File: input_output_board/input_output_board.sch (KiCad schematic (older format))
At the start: 18 parts, among them J1 Neutrik_NCJ6FA-H, J2 Neutrik_NCJ6FA-H, J3 Neutrik_NCJ6FA-H, J4 Neutrik_NCJ6FA-H, J5 AudioJack3, J6 Conn_02x05_Odd_Even, J7 Molex_SL_01x04_Male, J8 Molex_SL_01x04_Male, K1 G6S-2, K2 G6S-2, K3 G6S-2, K4 G6S-2, K5 G6S-2

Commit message: remove shield from internal audio connectors, change internal audio connectors to 1x2, and split input shields into four separate nets (one for each input)
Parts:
- J7: value Molex_SL_01x04_Male -> Molex_SL_01x02_Male; footprint Connector_Molex_SL:Molex_SL_A-70543-0003_1x04_P2.54mm_Vertical -> Connector_Molex_SL:Molex_SL_A-70543-0001_1x02_P2.54mm_Vertical; symbol Connector_gkeeth:Molex_SL_01x04_Male -> Connector_gkeeth:Molex_SL_01x02_Male; Distributor PN WM4802-ND -> (none); URL https://www.digikey.com/products/en?keywords=0705430003 -> (none); Unit Price 0.99 -> (none)
- J8: value Molex_SL_01x04_Male -> Molex_SL_01x02_Male; footprint Connector_Molex_SL:Molex_SL_A-70543-0003_1x04_P2.54mm_Vertical -> Connector_Molex_SL:Molex_SL_A-70543-0001_1x02_P2.54mm_Vertical; symbol Connector_gkeeth:Molex_SL_01x04_Male -> Connector_gkeeth:Molex_SL_01x02_Male; Distributor PN WM4802-ND -> (none); Manufacturer PN 0705430003 -> 0705430001; URL https://www.digikey.com/products/en?keywords=0705430003 -> (none); Unit Price 0.99 -> (none)
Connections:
- net input_selected_cold: now also J7.2 (Pin_2); no longer J7.4 (Pin_4)
- net output_cold: now also J8.2 (Pin_2); no longer J8.4 (Pin_4)
- net output_shield: no longer J8.2 (Pin_2), J8.3 (Pin_3)
- removed net input_shield: J1.1, J1.G, J1.S, J2.1, J2.G, J2.S, J3.1, J3.G, J3.S, J4.1, J4.G, J4.S, J7.2 (Pin_2), J7.3 (Pin_3)
- new net input1_shield: J1.1, J1.G, J1.S
- new net input2_shield: J2.1, J2.G, J2.S
- new net input3_shield: J3.1, J3.G, J3.S
- new net input4_shield: J4.1, J4.G, J4.S
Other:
- note added: "Shields & XLR case ground bonded DIRECTLY to chassis at each connector:\n - XLR combo connectors via mounting screw holes\n - phono jack via chassis contact\n\nflood input_shield across all inputs"
- note added: "output shield connected to chassis by output connector"
- note removed: "Shields & XLR case ground bonded DIRECTLY to chassis at each connector:\n - XLR combo connectors via mounting screw holes\n - phono jack via chassis contact\n\nflood input_shield across all inputs and connect to input connector (J7)"
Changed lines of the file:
@@
 	2450 3750 2450 3850
 Text Label 2000 5200 2    50   ~ 0
-input_shield
+input3_shield
 Text Label 2900 5200 0    50   ~ 0
 input3_hot
@@
 	2150 5200 2050 5200
 Wire Wire Line
-	8200 5850 7300 5850
+	8200 5650 7300 5650
 Text Label 7500 5550 0    50   ~ 0
 output_hot
-Text Label 7500 5850 0    50   ~ 0
+Text Label 7500 5650 0    50   ~ 0
 output_cold
-Wire Wire Line
-	7300 5750 7400 5750
-Wire Wire Line
-	7300 5650 7400 5650
-Wire Wire Line
-	7400 5650 7400 5750
-Connection ~ 7400 5750
-Wire Wire Line
-	7400 5750 8050 5750
-Text Label 7500 5750 0    50   ~ 0
-output_shield
 Wire Wire Line
 	2000 1600 1400 1600
@@
 $EndComp
 $Comp
-L Connector_gkeeth:Molex_SL_01x04_Male J7
+L Connector_gkeeth:Molex_SL_01x02_Male J7
 U 1 1 5CB530B8
-P 6500 4250
-F 0 "J7" H 6472 4224 50  0000 R CNN
-F 1 "Molex_SL_01x04_Male" H 6472 4133 50  0000 R CNN
-F 2 "Connector_Molex_SL:Molex_SL_A-70543-0003_1x04_P2.54mm_Vertical" H 6500 4250 50  0001 C CNN
-F 3 "https://www.molex.com/pdm_docs/sd/705430001_sd.pdf" H 6500 4250 50  0001 C CNN
-F 4 "Molex" H 6500 4250 50  0001 C CNN "Manufacturer"
-F 5 "0705430003" H 6500 4250 50  0001 C CNN "Manufacturer PN"
-F 6 "Digikey" H 6500 4250 50  0001 C CNN "Distributor"
-F 7 "WM4802-ND" H 6500 4250 50  0001 C CNN "Distributor PN"
-F 8 "https://www.digikey.com/products/en?keywords=0705430003" H 6500 4250 50  0001 C CNN "URL"
-F 9 "0.99" H 6500 4250 50  0001 C CNN "Unit Price"
-	1    6500 4250
+P 6500 4150
+F 0 "J7" H 6472 4124 50  0000 R CNN
+F 1 "Molex_SL_01x02_Male" H 6472 4033 50  0000 R CNN
+F 2 "Connector_Molex_SL:Molex_SL_A-70543-0001_1x02_P2.54mm_Vertical" H 6500 4150 50  0001 C CNN
+F 3 "https://www.molex.com/pdm_docs/sd/705430001_sd.pdf" H 6500 4150 50  0001 C CNN
+F 4 "Molex" H 6500 4150 50  0001 C CNN "Manufacturer"
+F 5 "0705430003" H 6500 4150 50  0001 C CNN "Manufacturer PN"
+F 6 "Digikey" H 6500 4150 50  0001 C CNN "Distributor"
+	1    6500 4150
 	-1   0    0    -1
 $EndComp
 Text Label 5450 4250 0    50   ~ 0
-input_shield
-Wire Wire Line
-	6200 4250 6300 4250
-Connection ~ 6200 4250
-Wire Wire Line
-	6200 4350 6300 4350
-Wire Wire Line
-	6200 4250 6200 4350
-Text Label 5450 4450 0    50   ~ 0
 input_selected_cold
 Text Label 5450 4150 0    50   ~ 0
 input_selected_hot
 Text Label 2000 3450 2    50   ~ 0
-input_shield
+input2_shield
 Text Label 2000 3250 2    50   ~ 0
 input2_hot
@@
 input3_hot
 Text Label 2000 1700 2    50   ~ 0
-input_shield
+input1_shield
 Text Label 2000 1600 2    50   ~ 0
 input1_cold
@@
 	9200 5750 9400 5750
 Wire Wire Line
-	8200 5850 8200 5950
+	8200 5650 8200 5950
 Wire Wire Line
 	8200 5950 8400 5950
@@
 	7300 5550 8400 5550
 Wire Wire Line
-	8050 5750 8050 6350
-Wire Wire Line
-	8050 6350 9300 6350
-Wire Wire Line
-	9300 6350 9300 5850
+	8050 6450 9300 6450
+Wire Wire Line
+	9300 6450 9300 5850
 Wire Wire Line
 	9300 5850 9400 5850
@@
 Connection ~ 8200 2650
 Text Notes 7500 3950 0    50   ~ 0
-Shields & XLR case ground bonded DIRECTLY to chassis at each connector:\n - XLR combo connectors via mounting screw holes\n - phono jack via chassis contact\n\nflood input_shield across all inputs and connect to input connector (J7)
+Shields & XLR case ground bonded DIRECTLY to chassis at each connector:\n - XLR combo connectors via mounting screw holes\n - phono jack via chassis contact\n\nflood input_shield across all inputs
 Wire Wire Line
 	2350 2100 2350 2000
@@
 	2050 7350 2350 7350
 Text Label 2000 6950 2    50   ~ 0
-input_shield
+input4_shield
 Wire Wire Line
 	2450 7250 2450 7350
@@
 	5000 2000 4300 2000
 Wire Wire Line
-	6300 4450 5000 4450
+	6300 4250 5000 4250
 Text Notes 700  7850 0    79   Italic 16
 INPUT CONNECTORS / RELAYS
@@
 Wire Notes Line
 	650  7900 650  550
-Wire Wire Line
-	5450 4250 6200 4250
 Wire Notes Line
 	750  2300 750  650
@@
 	5650 4850 5650 7900
 Wire Wire Line
-	5000 5500 5000 4450
-Connection ~ 5000 4450
+	5000 5500 5000 4250
+Connection ~ 5000 4250
 Wire Wire Line
 	5000 3750 5000 2000
@@
 $EndComp
 $Comp
-L Connector_gkeeth:Molex_SL_01x04_Male J8
+L Connector_gkeeth:Molex_SL_01x02_Male J8
 U 1 1 5CEEDB20
-P 7100 5650
-F 0 "J8" H 7072 5624 50  0000 R CNN
-F 1 "Molex_SL_01x04_Male" H 7072 5533 50  0000 R CNN
-F 2 "Connector_Molex_SL:Molex_SL_A-70543-0003_1x04_P2.54mm_Vertical" H 7100 5650 50  0001 C CNN
-F 3 "https://www.molex.com/pdm_docs/sd/705430001_sd.pdf" H 7100 5650 50  0001 C CNN
-F 4 "Molex" H 7100 5650 50  0001 C CNN "Manufacturer"
-F 5 "0705430003" H 7100 5650 50  0001 C CNN "Manufacturer PN"
-F 6 "Digikey" H 7100 5650 50  0001 C CNN "Distributor"
-F 7 "WM4802-ND" H 7100 5650 50  0001 C CNN "Distributor PN"
-F 8 "https://www.digikey.com/products/en?keywords=0705430003" H 7100 5650 50  0001 C CNN "URL"
-F 9 "0.99" H 7100 5650 50  0001 C CNN "Unit Price"
-	1    7100 5650
-	1    0    0    -1
-$EndComp
-Wire Wire Line
-	5000 3750 5000 4450
+P 7100 5550
+F 0 "J8" H 7072 5524 50  0000 R CNN
+F 1 "Molex_SL_01x02_Male" H 7072 5433 50  0000 R CNN
+F 2 "Connector_Molex_SL:Molex_SL_A-70543-0001_1x02_P2.54mm_Vertical" H 7100 5550 50  0001 C CNN
+F 3 "https://www.molex.com/pdm_docs/sd/705430001_sd.pdf" H 7100 5550 50  0001 C CNN
+F 4 "Molex" H 7100 5550 50  0001 C CNN "Manufacturer"
+F 5 "0705430001" H 7100 5550 50  0001 C CNN "Manufacturer PN"
+F 6 "Digikey" H 7100 5550 50  0001 C CNN "Distributor"
+	1    7100 5550
+	1    0    0    -1
+$EndComp
+Wire Wire Line
+	5000 3750 5000 4250
 Wire Wire Line
 	5150 4150 6300 4150
@@
 Wire Wire Line
 	1400 1700 2050 1700
+Text Label 8050 6450 0    50   ~ 0
+output_shield
+Text Notes 7750 6550 0    50   ~ 0
+output shield connected to chassis by output connector
 $EndSCHEMATC

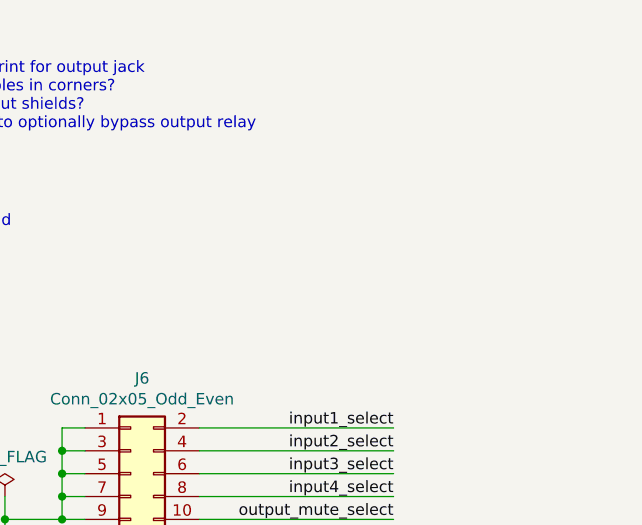
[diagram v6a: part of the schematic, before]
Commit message: add license info to schematics & layouts, including made with kicad logo, as well as project info to silkscreen
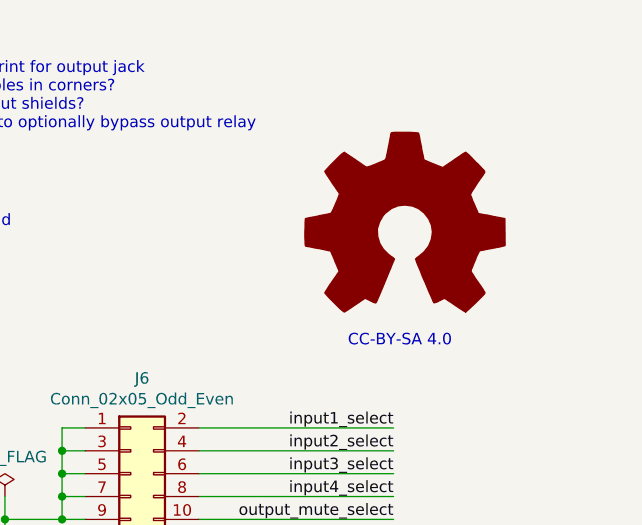
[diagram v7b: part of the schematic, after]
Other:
- note added: "CC-BY-SA 4.0"
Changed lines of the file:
@@
 Text Notes 7750 6550 0    50   ~ 0
 output shield connected to chassis by output connector
+$Comp
+L Graphic:Logo_Open_Hardware_Large #LOGO?
+U 1 1 5D0E77C4
+P 9950 1400
+F 0 "#LOGO?" H 9950 1900 50  0001 C CNN
+F 1 "Logo_Open_Hardware_Large" H 9950 1000 50  0001 C CNN
+F 2 "" H 9950 1400 50  0001 C CNN
+F 3 "~" H 9950 1400 50  0001 C CNN
+	1    9950 1400
+	1    0    0    -1
+$EndComp
+Text Notes 9700 1900 0    50   ~ 0
+CC-BY-SA 4.0
 $EndSCHEMATC
